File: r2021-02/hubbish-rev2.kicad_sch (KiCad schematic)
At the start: 4 parts

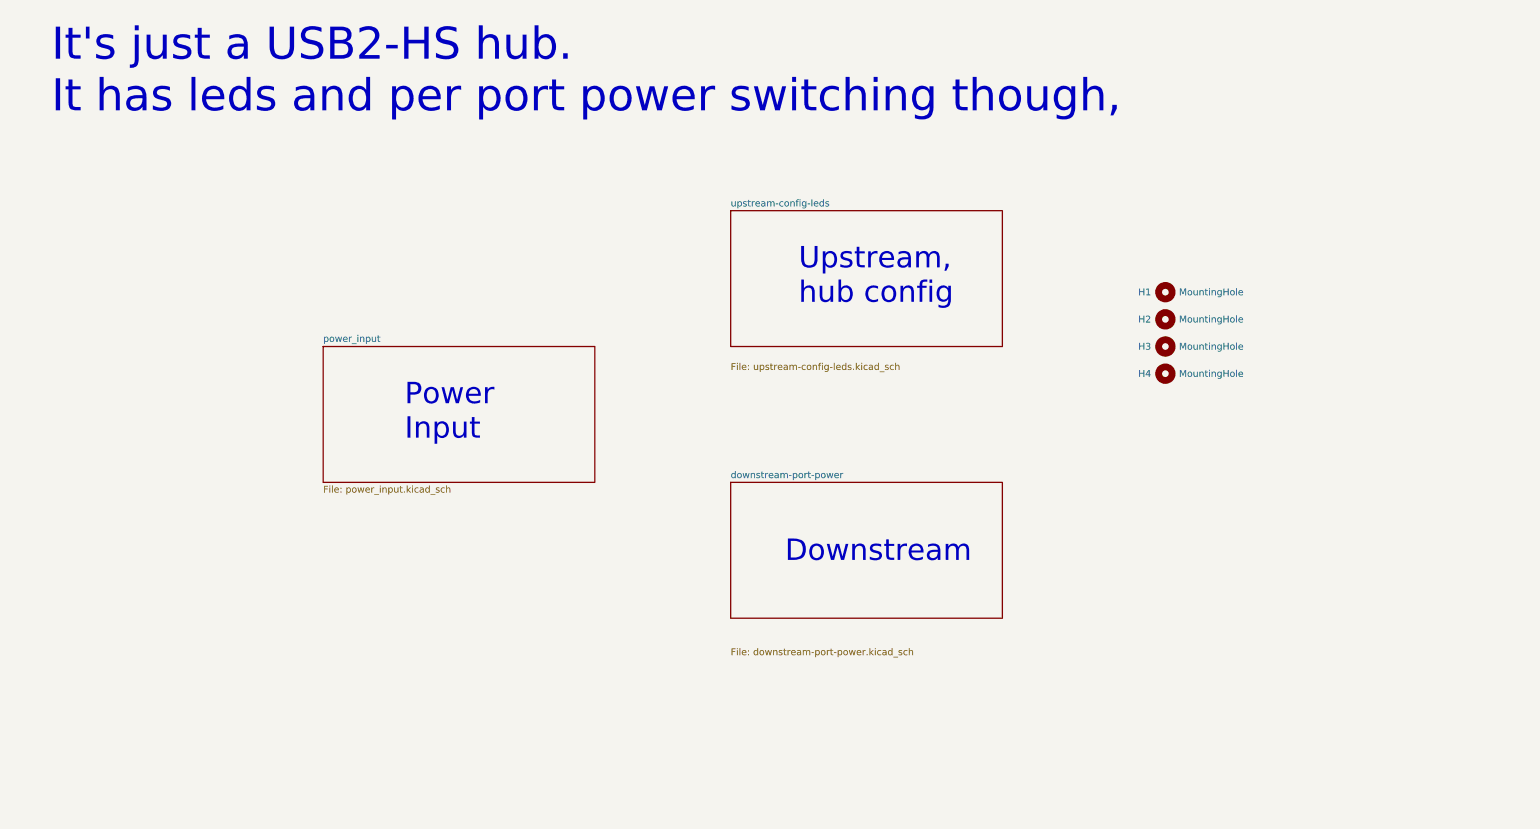
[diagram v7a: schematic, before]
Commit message: hw: r2: clarify parts and values for polarity protection
falstad simulation:

$ 1 0.000005 10.20027730826997 50 5 50 5e-11
34 zener-5.6 1 1.7143528192810002e-7 0 2.0000000000000084 10 1
z 416 208 416 128 2 zener-5.6
f 288 208 288 128 33 1.5 0.02
r 288 256 288 304 0 10000
r 528 144 528 304 0 10
w 304 128 416 128 0
w 288 208 288 224 0
w 416 128 528 144 0
w 416 208 288 208 0
w 528 304 288 304 0
v 64 224 64 160 0 0 40 30 0 0 0.5
w 160 112 272 128 0
w 128 304 288 304 0
v 112 160 112 224 0 0 40 12 0 0 0.5
w 64 224 128 304 0
w 112 224 128 304 0
S 160 112 112 112 0 1 false 0 2
w 112 128 112 160 0
w 112 96 64 160 0
368 272 128 272 64 0 0
368 416 128 368 64 0 0
p 288 208 416 128 1 0 0
370 288 224 288 256 1 0 0
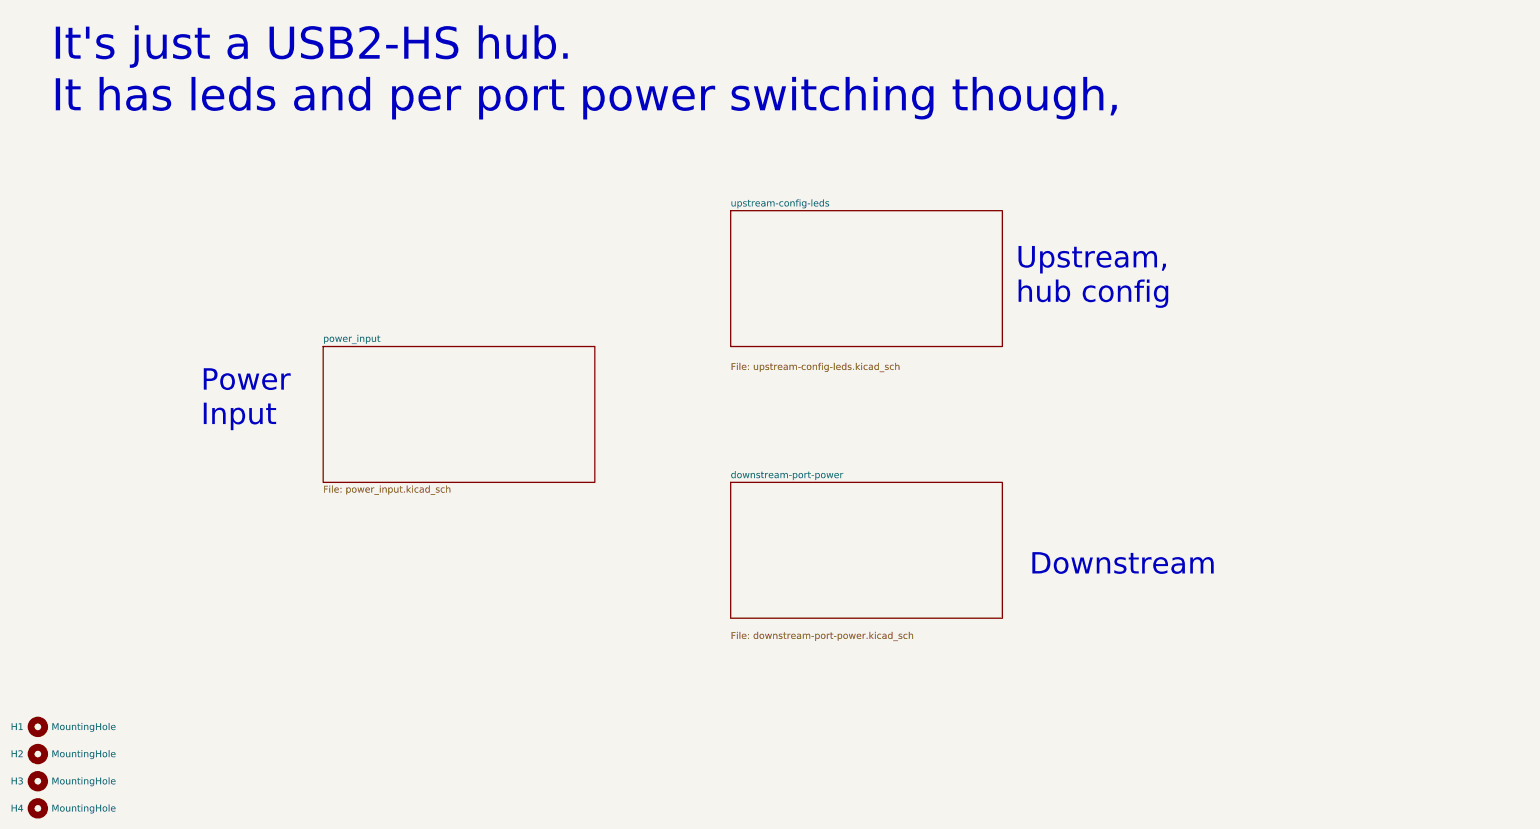
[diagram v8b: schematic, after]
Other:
- moved on the sheet: H1, H2, H3, H4
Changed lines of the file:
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@@
     (comment 4 "github.com/karlp/hubbish")
   )
-  (text "Upstream, \nhub config" (at 165.1 93.98 0)
+  (text "Upstream, \nhub config" (at 205.74 93.98 0)
     (effects (font (size 4 4)) (justify left bottom))
   )
-  (text "Downstream" (at 162.56 142.24 0)
+  (text "Downstream" (at 208.28 144.78 0)
     (effects (font (size 4 4)) (justify left bottom))
   )
-  (text "Power\nInput" (at 91.44 119.38 0)
+  (text "Power\nInput" (at 53.34 116.84 0)
     (effects (font (size 4 4)) (justify left bottom))
   )
@@
     (effects (font (size 5.994 5.994)) (justify left bottom))
   )
-  (symbol (lib_id "Mechanical:MountingHole") (at 233.68 91.44 0) (unit 1)
+  (symbol (lib_id "Mechanical:MountingHole") (at 22.86 172.72 0) (unit 1)
     (in_bom yes) (on_board yes)
-    (property "Reference" "H1" (id 0) (at 228.6 91.44 0)
-      (effects (font (size 1.27 1.27)) (justify left))
-    )
-    (property "Value" "MountingHole" (id 1) (at 236.22 91.44 0)
-      (effects (font (size 1.27 1.27)) (justify left))
-    )
-    (property "Footprint" "MountingHole:MountingHole_2.7mm_M2.5" (id 2) (at 233.68 91.44 0)
-      (effects (font (size 1.27 1.27)) hide)
-    )
-    (property "Datasheet" "~" (id 3) (at 233.68 91.44 0)
-      (effects (font (size 1.27 1.27)) hide)
-    )
-  )
-  (symbol (lib_id "Mechanical:MountingHole") (at 233.68 96.52 0) (unit 1)
+    (property "Reference" "H1" (id 0) (at 17.78 172.72 0)
+      (effects (font (size 1.27 1.27)) (justify left))
+    )
+    (property "Value" "MountingHole" (id 1) (at 25.4 172.72 0)
+      (effects (font (size 1.27 1.27)) (justify left))
+    )
+    (property "Footprint" "MountingHole:MountingHole_2.7mm_M2.5" (id 2) (at 22.86 172.72 0)
+      (effects (font (size 1.27 1.27)) hide)
+    )
+    (property "Datasheet" "~" (id 3) (at 22.86 172.72 0)
+      (effects (font (size 1.27 1.27)) hide)
+    )
+  )
+  (symbol (lib_id "Mechanical:MountingHole") (at 22.86 177.8 0) (unit 1)
     (in_bom yes) (on_board yes)
-    (property "Reference" "H2" (id 0) (at 228.6 96.52 0)
-      (effects (font (size 1.27 1.27)) (justify left))
-    )
-    (property "Value" "MountingHole" (id 1) (at 236.22 96.52 0)
-      (effects (font (size 1.27 1.27)) (justify left))
-    )
-    (property "Footprint" "MountingHole:MountingHole_2.7mm_M2.5" (id 2) (at 233.68 96.52 0)
-      (effects (font (size 1.27 1.27)) hide)
-    )
-    (property "Datasheet" "~" (id 3) (at 233.68 96.52 0)
-      (effects (font (size 1.27 1.27)) hide)
-    )
-  )
-  (symbol (lib_id "Mechanical:MountingHole") (at 233.68 101.6 0) (unit 1)
+    (property "Reference" "H2" (id 0) (at 17.78 177.8 0)
+      (effects (font (size 1.27 1.27)) (justify left))
+    )
+    (property "Value" "MountingHole" (id 1) (at 25.4 177.8 0)
+      (effects (font (size 1.27 1.27)) (justify left))
+    )
+    (property "Footprint" "MountingHole:MountingHole_2.7mm_M2.5" (id 2) (at 22.86 177.8 0)
+      (effects (font (size 1.27 1.27)) hide)
+    )
+    (property "Datasheet" "~" (id 3) (at 22.86 177.8 0)
+      (effects (font (size 1.27 1.27)) hide)
+    )
+  )
+  (symbol (lib_id "Mechanical:MountingHole") (at 22.86 182.88 0) (unit 1)
     (in_bom yes) (on_board yes)
-    (property "Reference" "H3" (id 0) (at 228.6 101.6 0)
-      (effects (font (size 1.27 1.27)) (justify left))
-    )
-    (property "Value" "MountingHole" (id 1) (at 236.22 101.6 0)
-      (effects (font (size 1.27 1.27)) (justify left))
-    )
-    (property "Footprint" "MountingHole:MountingHole_2.7mm_M2.5" (id 2) (at 233.68 101.6 0)
-      (effects (font (size 1.27 1.27)) hide)
-    )
-    (property "Datasheet" "~" (id 3) (at 233.68 101.6 0)
-      (effects (font (size 1.27 1.27)) hide)
-    )
-  )
-  (symbol (lib_id "Mechanical:MountingHole") (at 233.68 106.68 0) (unit 1)
+    (property "Reference" "H3" (id 0) (at 17.78 182.88 0)
+      (effects (font (size 1.27 1.27)) (justify left))
+    )
+    (property "Value" "MountingHole" (id 1) (at 25.4 182.88 0)
+      (effects (font (size 1.27 1.27)) (justify left))
+    )
+    (property "Footprint" "MountingHole:MountingHole_2.7mm_M2.5" (id 2) (at 22.86 182.88 0)
+      (effects (font (size 1.27 1.27)) hide)
+    )
+    (property "Datasheet" "~" (id 3) (at 22.86 182.88 0)
+      (effects (font (size 1.27 1.27)) hide)
+    )
+  )
+  (symbol (lib_id "Mechanical:MountingHole") (at 22.86 187.96 0) (unit 1)
     (in_bom yes) (on_board yes)
-    (property "Reference" "H4" (id 0) (at 228.6 106.68 0)
-      (effects (font (size 1.27 1.27)) (justify left))
-    )
-    (property "Value" "MountingHole" (id 1) (at 236.22 106.68 0)
-      (effects (font (size 1.27 1.27)) (justify left))
-    )
-    (property "Footprint" "MountingHole:MountingHole_2.7mm_M2.5" (id 2) (at 233.68 106.68 0)
-      (effects (font (size 1.27 1.27)) hide)
-    )
-    (property "Datasheet" "~" (id 3) (at 233.68 106.68 0)
+    (property "Reference" "H4" (id 0) (at 17.78 187.96 0)
+      (effects (font (size 1.27 1.27)) (justify left))
+    )
+    (property "Value" "MountingHole" (id 1) (at 25.4 187.96 0)
+      (effects (font (size 1.27 1.27)) (justify left))
+    )
+    (property "Footprint" "MountingHole:MountingHole_2.7mm_M2.5" (id 2) (at 22.86 187.96 0)
+      (effects (font (size 1.27 1.27)) hide)
+    )
+    (property "Datasheet" "~" (id 3) (at 22.86 187.96 0)
       (effects (font (size 1.27 1.27)) hide)
     )
@@
       (effects (font (size 1.27 1.27)) (justify left bottom))
     )
-    (property "Sheetfile" "downstream-port-power.kicad_sch" (id 1) (at 152.4 157.9885 0)
+    (property "Sheetfile" "downstream-port-power.kicad_sch" (id 1) (at 152.4 154.94 0)
       (effects (font (size 1.27 1.27)) (justify left top))
     )
@@
       (reference "D11") (unit 1) (value "LTST-C295KGKRKT") (footprint "LED_SMD:LED_LiteOn_LTST-C295K")
     )
-    (path "/152e32c2-e0fb-44f8-8d88-d6407d12d020/1195ccd8-3742-46a6-ad73-60c1988000a6"
-      (reference "D?") (unit 1) (value "6.8V Zener or so") (footprint "Diode_SMD:D_SOD-123F")
+    (path "/152e32c2-e0fb-44f8-8d88-d6407d12d020/413dc7fc-240c-4452-bbbf-3fc6575124cb"
+      (reference "D?") (unit 1) (value "BZT52B12") (footprint "Diode_SMD:D_SOD-123")
     )
     (path "/152e32c2-e0fb-44f8-8d88-d6407d12d020/6992f78d-92d0-485b-ab69-838dc56bfa1c"
@@
     )
     (path "/152e32c2-e0fb-44f8-8d88-d6407d12d020/47c39ff5-72fc-46d9-9120-31b9f4134d63"
-      (reference "R?") (unit 1) (value "330") (footprint "Resistor_SMD:R_0603_1608Metric")
+      (reference "R?") (unit 1) (value "10k") (footprint "Resistor_SMD:R_0603_1608Metric")
     )
     (path "/152e32c2-e0fb-44f8-8d88-d6407d12d020/4a9d37e3-02ae-4d78-8c7e-57b14375fb87"
